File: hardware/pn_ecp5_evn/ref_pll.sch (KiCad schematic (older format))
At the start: 38 parts, among them J601 Conn_Coaxial, U601 LM2904, U602 OPA2211, X601 ABLNO

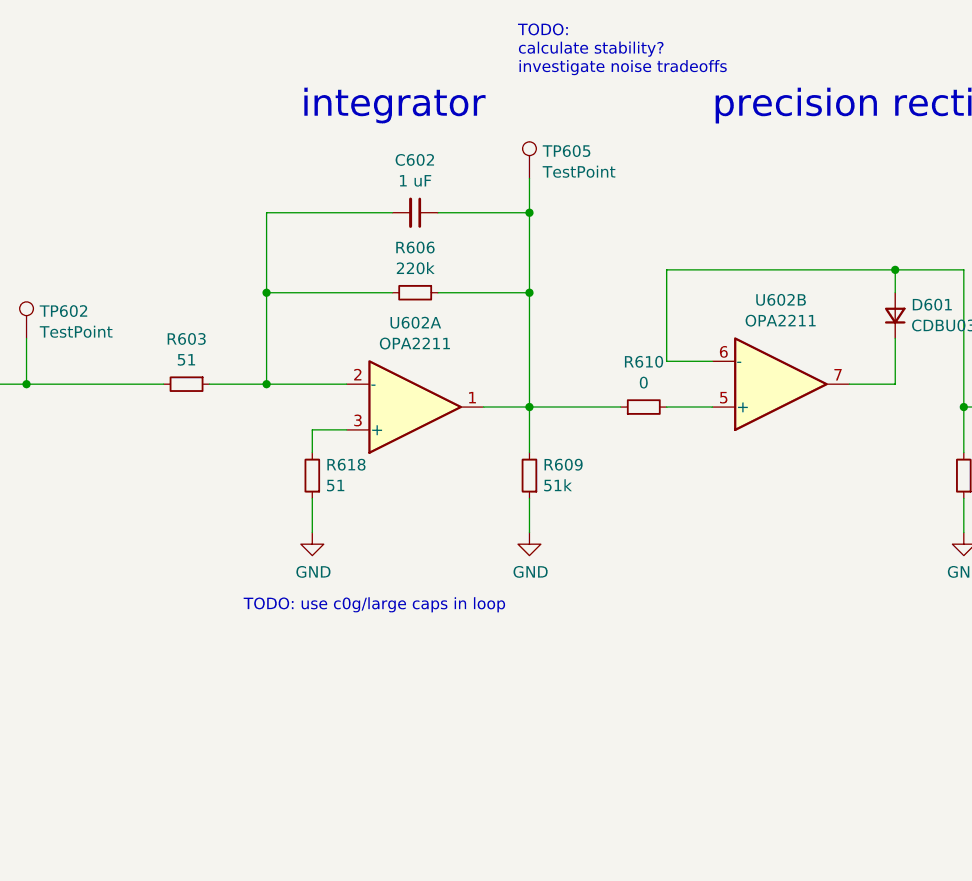
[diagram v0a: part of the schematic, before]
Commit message: fix integrator in reference pll..
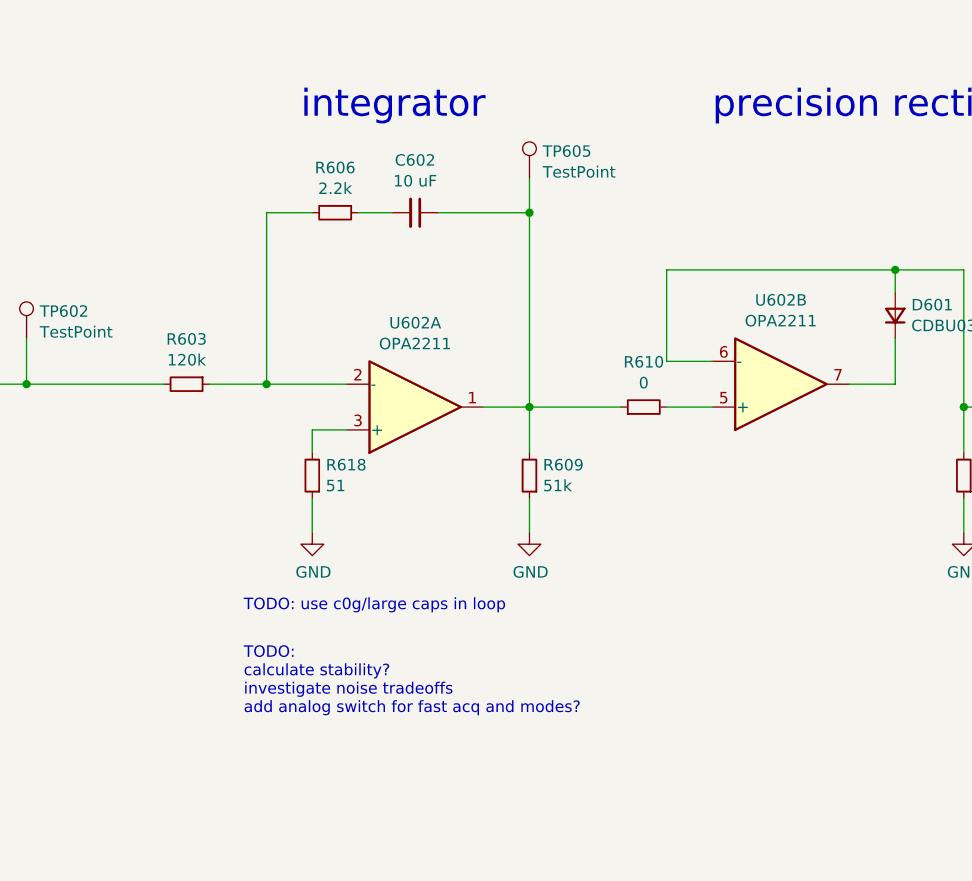
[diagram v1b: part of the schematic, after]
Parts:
- C602: value 1 uF -> 10 uF
- R603: value 51 -> 120k
- R606: value 220k -> 2.2k
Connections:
- net at R603.1, R606.2, U602.2 (-): no longer C602.2
- net at C602.1, R609.2, R610.1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: no longer R606.1
- new net: C602.2, R606.1
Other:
- note added: "TODO:\ncalculate stability?\ninvestigate noise tradeoffs\nadd analog switch for fast acq and modes?"
- note removed: "TODO:\ncalculate stability?\ninvestigate noise tradeoffs"
- moved on the sheet: R606
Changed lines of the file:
@@
 AR Path="/5F4ECD93/5F4F273D" Ref="R603"  Part="1"
 F 0 "R603" V 2454 2300 50  0000 C CNN
-F 1 "51" V 2545 2300 50  0000 C CNN
+F 1 "120k" V 2545 2300 50  0000 C CNN
 F 2 "Resistor_SMD:R_0402_1005Metric" H 2650 2300 50  0001 C CNN
 F 3 "~" H 2650 2300 50  0001 C CNN
@@
 L Device:R_Small R?
 U 1 1 5F4F2753
-P 3650 1900
+P 3300 1550
 AR Path="/5F265927/5F4F2753" Ref="R?"  Part="1"
 AR Path="/5F4ECD93/5F4F2753" Ref="R606"  Part="1"
-F 0 "R606" V 3454 1900 50  0000 C CNN
-F 1 "220k" V 3545 1900 50  0000 C CNN
-F 2 "Resistor_SMD:R_0402_1005Metric" H 3650 1900 50  0001 C CNN
-F 3 "~" H 3650 1900 50  0001 C CNN
-F 4 "N/A" H 3650 1900 50  0001 C CNN "Distributor Part Number"
-	1    3650 1900
+F 0 "R606" V 3104 1550 50  0000 C CNN
+F 1 "2.2k" V 3195 1550 50  0000 C CNN
+F 2 "Resistor_SMD:R_0402_1005Metric" H 3300 1550 50  0001 C CNN
+F 3 "~" H 3300 1550 50  0001 C CNN
+F 4 "N/A" H 3300 1550 50  0001 C CNN "Distributor Part Number"
+	1    3300 1550
 	0    1    1    0
 $EndComp
@@
 AR Path="/5F4ECD93/5F4F2759" Ref="C602"  Part="1"
 F 0 "C602" V 3421 1550 50  0000 C CNN
-F 1 "1 uF" V 3512 1550 50  0000 C CNN
+F 1 "10 uF" V 3512 1550 50  0000 C CNN
 F 2 "Capacitor_SMD:C_0603_1608Metric" H 3650 1550 50  0001 C CNN
 F 3 "~" H 3650 1550 50  0001 C CNN
@@
 $EndComp
 Wire Wire Line
-	3750 1900 4150 1900
-Wire Wire Line
 	3750 1550 4150 1550
 Wire Wire Line
-	4150 1550 4150 1900
-Wire Wire Line
-	3550 1550 3000 1550
-Wire Wire Line
-	3000 1550 3000 1900
-Wire Wire Line
-	3550 1900 3000 1900
+	3200 1550 3000 1550
 $Comp
 L Device:R_Small R?
@@
 Wire Wire Line
 	2750 2300 3000 2300
-Wire Wire Line
-	4150 1900 4150 2400
-Connection ~ 4150 1900
-Wire Wire Line
-	3000 1900 3000 2300
-Connection ~ 3000 1900
 Connection ~ 3000 2300
 Wire Wire Line
@@
 Text HLabel 1700 2300 0    50   Input ~ 0
 PHDET_IN
-Text Notes 4100 950  0    50   ~ 0
-TODO:\ncalculate stability?\ninvestigate noise tradeoffs
+Text Notes 2900 3750 0    50   ~ 0
+TODO:\ncalculate stability?\ninvestigate noise tradeoffs\nadd analog switch for fast acq and modes?
 Text Notes 2600 4900 0    50   ~ 0
 TODO:\nverify buffer circuit
@@
 	6050 1800 6050 2400
 Connection ~ 5750 1800
+Wire Wire Line
+	3000 1550 3000 2300
+Wire Wire Line
+	3400 1550 3550 1550
+Wire Wire Line
+	4150 1550 4150 2400
 $EndSCHEMATC
